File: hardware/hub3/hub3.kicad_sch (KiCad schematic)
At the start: 7 parts, among them J1 LCD0, J2 LCD1, J3 LCD2, U1 74HC138, U2 XIAO ESP32S3

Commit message: hub3: use the Ckmtw C132515 FFC connector, 44 mm board
C132515 has JLCPCB's own EasyEDA footprint, so the pads come from it
rather than from pixels of a drawing. Its body is 2.5 mm longer, so the
board grows to 44 mm to keep the corners clear. Move the 10 uF next to
the XIAO 5V pin.

route.py now starts each attempt from an unrouted copy that make.py
leaves in build/ with the project beside it (without it pcbnew used the
default net classes and saved them over the project), and when an
attempt is not clean it makes the board again: Freerouting routes the
same DSN the same way whatever its options, but each make.py run gives
a different DSN. Allow 7.5 mm of necked power track, about 2.5 mm per
connector.

Claude-Session: https://claude.ai/code/session_01QQqL2MiTqB6ZDq8JiNUdWg
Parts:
- J1, J2, J3: footprint cubic-earth:FFC_1.0mm_20P_Bottom_C2998680 -> cubic-earth:FFC_1.0mm_20P_Bottom_C132515; LCSC C2998680 -> C132515
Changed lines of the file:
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@@
 (property "Reference" "J1" (at 40.64 111.76 0) (effects (font (size 1.27 1.27))))
 (property "Value" "LCD0" (at 40.64 167.64 0) (effects (font (size 1.27 1.27))))
-(property "Footprint" "cubic-earth:FFC_1.0mm_20P_Bottom_C2998680" (at 40.64 139.70 0) (effects (font (size 1.27 1.27)) hide))
+(property "Footprint" "cubic-earth:FFC_1.0mm_20P_Bottom_C132515" (at 40.64 139.70 0) (effects (font (size 1.27 1.27)) hide))
 (property "Datasheet" "" (at 40.64 139.70 0) (effects (font (size 1.27 1.27)) hide))
-(property "LCSC" "C2998680" (at 40.64 139.70 0) (effects (font (size 1.27 1.27)) hide))
+(property "LCSC" "C132515" (at 40.64 139.70 0) (effects (font (size 1.27 1.27)) hide))
 (pin "1")
 (pin "2")
@@
 (pin "19")
 (pin "20")
-(instances (project "hub3" (path "/b9e327cf-b8af-4256-b178-5e44f1f45300" (reference "J1") (unit 1)))))
+(instances (project "hub3" (path "/f0ae39f4-92a4-45e5-bc8c-1e4964e93c33" (reference "J1") (unit 1)))))
 (global_label "GND" (shape passive) (at 35.56 115.57 180) (effects (font (size 1.27 1.27)) (justify right)))
 (global_label "GND" (shape passive) (at 35.56 118.11 180) (effects (font (size 1.27 1.27)) (justify right)))
@@
 (property "Reference" "J2" (at 99.06 111.76 0) (effects (font (size 1.27 1.27))))
 (property "Value" "LCD1" (at 99.06 167.64 0) (effects (font (size 1.27 1.27))))
-(property "Footprint" "cubic-earth:FFC_1.0mm_20P_Bottom_C2998680" (at 99.06 139.70 0) (effects (font (size 1.27 1.27)) hide))
+(property "Footprint" "cubic-earth:FFC_1.0mm_20P_Bottom_C132515" (at 99.06 139.70 0) (effects (font (size 1.27 1.27)) hide))
 (property "Datasheet" "" (at 99.06 139.70 0) (effects (font (size 1.27 1.27)) hide))
-(property "LCSC" "C2998680" (at 99.06 139.70 0) (effects (font (size 1.27 1.27)) hide))
+(property "LCSC" "C132515" (at 99.06 139.70 0) (effects (font (size 1.27 1.27)) hide))
 (pin "1")
 (pin "2")
@@
 (pin "19")
 (pin "20")
-(instances (project "hub3" (path "/b9e327cf-b8af-4256-b178-5e44f1f45300" (reference "J2") (unit 1)))))
+(instances (project "hub3" (path "/f0ae39f4-92a4-45e5-bc8c-1e4964e93c33" (reference "J2") (unit 1)))))
 (global_label "GND" (shape passive) (at 93.98 115.57 180) (effects (font (size 1.27 1.27)) (justify right)))
 (global_label "GND" (shape passive) (at 93.98 118.11 180) (effects (font (size 1.27 1.27)) (justify right)))
@@
 (property "Reference" "J3" (at 160.02 111.76 0) (effects (font (size 1.27 1.27))))
 (property "Value" "LCD2" (at 160.02 167.64 0) (effects (font (size 1.27 1.27))))
-(property "Footprint" "cubic-earth:FFC_1.0mm_20P_Bottom_C2998680" (at 160.02 139.70 0) (effects (font (size 1.27 1.27)) hide))
+(property "Footprint" "cubic-earth:FFC_1.0mm_20P_Bottom_C132515" (at 160.02 139.70 0) (effects (font (size 1.27 1.27)) hide))
 (property "Datasheet" "" (at 160.02 139.70 0) (effects (font (size 1.27 1.27)) hide))
-(property "LCSC" "C2998680" (at 160.02 139.70 0) (effects (font (size 1.27 1.27)) hide))
+(property "LCSC" "C132515" (at 160.02 139.70 0) (effects (font (size 1.27 1.27)) hide))
 (pin "1")
 (pin "2")
@@
 (pin "19")
 (pin "20")
-(instances (project "hub3" (path "/b9e327cf-b8af-4256-b178-5e44f1f45300" (reference "J3") (unit 1)))))
+(instances (project "hub3" (path "/f0ae39f4-92a4-45e5-bc8c-1e4964e93c33" (reference "J3") (unit 1)))))
 (global_label "GND" (shape passive) (at 154.94 115.57 180) (effects (font (size 1.27 1.27)) (justify right)))
 (global_label "GND" (shape passive) (at 154.94 118.11 180) (effects (font (size 1.27 1.27)) (justify right)))
@@
 (pin "8")
 (pin "9")
-(instances (project "hub3" (path "/b9e327cf-b8af-4256-b178-5e44f1f45300" (reference "U1") (unit 1)))))
+(instances (project "hub3" (path "/f0ae39f4-92a4-45e5-bc8c-1e4964e93c33" (reference "U1") (unit 1)))))
 (global_label "SEL_A" (shape passive) (at 119.38 60.96 180) (effects (font (size 1.27 1.27)) (justify right)))
 (global_label "LCD_CS2" (shape passive) (at 139.70 73.66 0) (effects (font (size 1.27 1.27)) (justify left)))
@@
 (pin "9")
 (pin "8")
-(instances (project "hub3" (path "/b9e327cf-b8af-4256-b178-5e44f1f45300" (reference "U2") (unit 1)))))
+(instances (project "hub3" (path "/f0ae39f4-92a4-45e5-bc8c-1e4964e93c33" (reference "U2") (unit 1)))))
 (global_label "SEL_A" (shape passive) (at 50.80 63.50 180) (effects (font (size 1.27 1.27)) (justify right)))
 (global_label "LCM_RESET" (shape passive) (at 50.80 66.04 180) (effects (font (size 1.27 1.27)) (justify right)))
@@
 (pin "1")
 (pin "2")
-(instances (project "hub3" (path "/b9e327cf-b8af-4256-b178-5e44f1f45300" (reference "C1") (unit 1)))))
+(instances (project "hub3" (path "/f0ae39f4-92a4-45e5-bc8c-1e4964e93c33" (reference "C1") (unit 1)))))
 (global_label "+3V3" (shape passive) (at 160.02 57.15 180) (effects (font (size 1.27 1.27)) (justify right)))
 (global_label "GND" (shape passive) (at 160.02 64.77 0) (effects (font (size 1.27 1.27)) (justify left)))
@@
 (pin "1")
 (pin "2")
-(instances (project "hub3" (path "/b9e327cf-b8af-4256-b178-5e44f1f45300" (reference "C2") (unit 1)))))
+(instances (project "hub3" (path "/f0ae39f4-92a4-45e5-bc8c-1e4964e93c33" (reference "C2") (unit 1)))))
 (global_label "+5V" (shape passive) (at 160.02 80.01 180) (effects (font (size 1.27 1.27)) (justify right)))
 (global_label "GND" (shape passive) (at 160.02 87.63 0) (effects (font (size 1.27 1.27)) (justify left)))

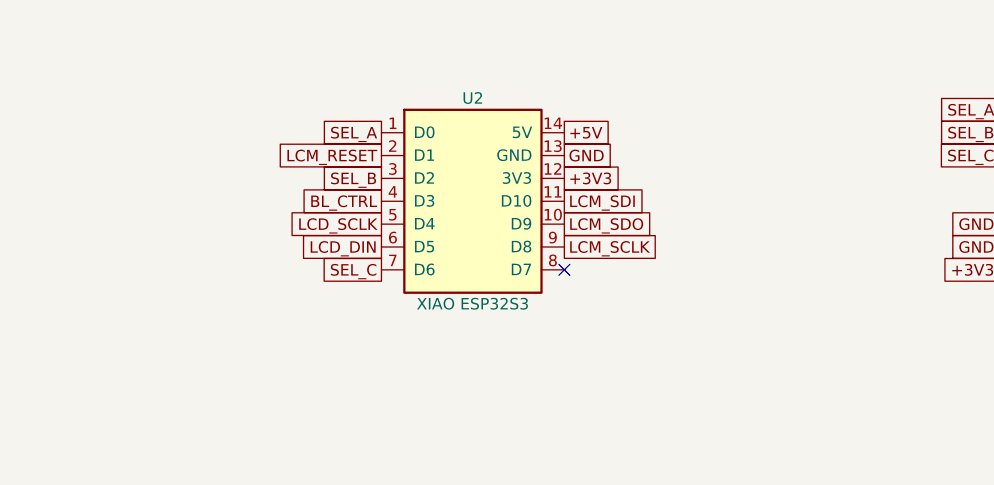
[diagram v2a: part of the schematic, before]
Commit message: hub3: assemble the XIAO's two pin sockets too
Replace the XIAO footprint with two 1x7 2.54 mm female sockets (J4, J5,
XFCN PM254V-11-07-H85, LCSC C2832270) for JLCPCB to fit. The XIAO
stays on the schematic but off the board; a board-only outline marks
where it sits and which row is D0 and which 5V. The placement file
gives the sockets' pad centre, since their origin is on pin 1. A test
checks the rows are 15.24 mm apart with D0 and 5V at the USB end.

Claude-Session: https://claude.ai/code/session_01QQqL2MiTqB6ZDq8JiNUdWg
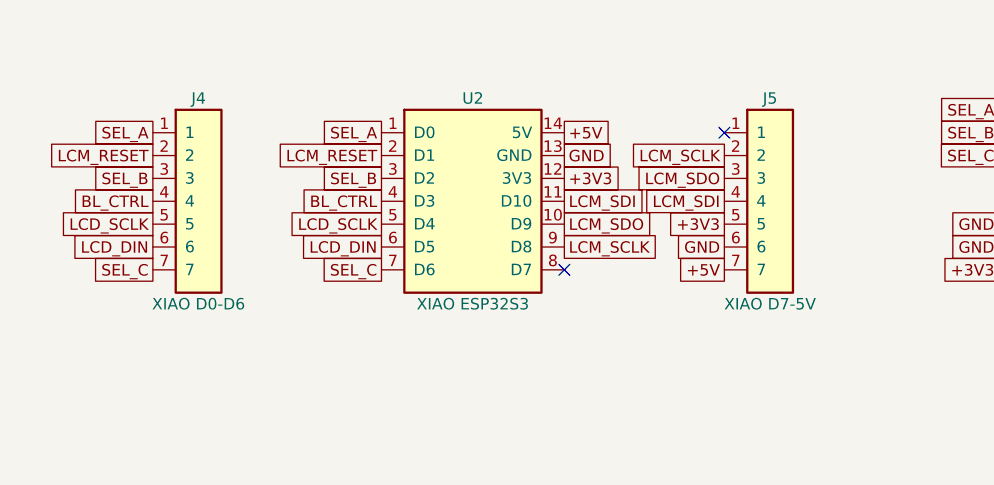
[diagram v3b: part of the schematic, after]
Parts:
- added J4: XIAO D0-D6, Connector_PinSocket_2.54mm:PinSocket_1x07_P2.54mm_Vertical, symbol cubic-earth:Socket_1x07
- added J5: XIAO D7-5V, Connector_PinSocket_2.54mm:PinSocket_1x07_P2.54mm_Vertical, symbol cubic-earth:Socket_1x07
- U2: footprint cubic-earth:XIAO_Socket_2x7_P2.54mm -> (none); now left out of the parts list
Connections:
- net +3V3: now also J5.5
- net +5V: now also J5.7
- net BL_CTRL: now also J4.4
- net GND: now also J5.6
- net LCD_DIN: now also J4.6
- net LCD_SCLK: now also J4.5
- net LCM_RESET: now also J4.2
- net LCM_SCLK: now also J5.2
- net LCM_SDI: now also J5.4
- net LCM_SDO: now also J5.3
- net SEL_A: now also J4.1
- net SEL_B: now also J4.3
- net SEL_C: now also J4.7
- no-connect marks 24 -> 25
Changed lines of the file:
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@@
 (pin "19")
 (pin "20")
-(instances (project "hub3" (path "/f0ae39f4-92a4-45e5-bc8c-1e4964e93c33" (reference "J1") (unit 1)))))
+(instances (project "hub3" (path "/a8cdc18e-1b7c-4f21-9802-1abcb25c4a52" (reference "J1") (unit 1)))))
 (global_label "GND" (shape passive) (at 35.56 115.57 180) (effects (font (size 1.27 1.27)) (justify right)))
 (global_label "GND" (shape passive) (at 35.56 118.11 180) (effects (font (size 1.27 1.27)) (justify right)))
@@
 (pin "19")
 (pin "20")
-(instances (project "hub3" (path "/f0ae39f4-92a4-45e5-bc8c-1e4964e93c33" (reference "J2") (unit 1)))))
+(instances (project "hub3" (path "/a8cdc18e-1b7c-4f21-9802-1abcb25c4a52" (reference "J2") (unit 1)))))
 (global_label "GND" (shape passive) (at 93.98 115.57 180) (effects (font (size 1.27 1.27)) (justify right)))
 (global_label "GND" (shape passive) (at 93.98 118.11 180) (effects (font (size 1.27 1.27)) (justify right)))
@@
 (pin "19")
 (pin "20")
-(instances (project "hub3" (path "/f0ae39f4-92a4-45e5-bc8c-1e4964e93c33" (reference "J3") (unit 1)))))
+(instances (project "hub3" (path "/a8cdc18e-1b7c-4f21-9802-1abcb25c4a52" (reference "J3") (unit 1)))))
 (global_label "GND" (shape passive) (at 154.94 115.57 180) (effects (font (size 1.27 1.27)) (justify right)))
 (global_label "GND" (shape passive) (at 154.94 118.11 180) (effects (font (size 1.27 1.27)) (justify right)))
@@
 (pin "8")
 (pin "9")
-(instances (project "hub3" (path "/f0ae39f4-92a4-45e5-bc8c-1e4964e93c33" (reference "U1") (unit 1)))))
+(instances (project "hub3" (path "/a8cdc18e-1b7c-4f21-9802-1abcb25c4a52" (reference "U1") (unit 1)))))
 (global_label "SEL_A" (shape passive) (at 119.38 60.96 180) (effects (font (size 1.27 1.27)) (justify right)))
 (global_label "LCD_CS2" (shape passive) (at 139.70 73.66 0) (effects (font (size 1.27 1.27)) (justify left)))
@@
 (global_label "GND" (shape passive) (at 129.54 83.82 0) (effects (font (size 1.27 1.27)) (justify left)))
 (no_connect (at 139.70 76.20))
-(symbol (lib_id "cubic-earth:XIAO_ESP32S3") (at 60.96 71.12 0) (unit 1) (exclude_from_sim no) (in_bom yes) (on_board yes) (dnp no)
+(symbol (lib_id "cubic-earth:XIAO_ESP32S3") (at 60.96 71.12 0) (unit 1) (exclude_from_sim no) (in_bom no) (on_board no) (dnp no)
 (property "Reference" "U2" (at 60.96 59.69 0) (effects (font (size 1.27 1.27))))
 (property "Value" "XIAO ESP32S3" (at 60.96 82.55 0) (effects (font (size 1.27 1.27))))
-(property "Footprint" "cubic-earth:XIAO_Socket_2x7_P2.54mm" (at 60.96 71.12 0) (effects (font (size 1.27 1.27)) hide))
+(property "Footprint" "" (at 60.96 71.12 0) (effects (font (size 1.27 1.27)) hide))
 (property "Datasheet" "" (at 60.96 71.12 0) (effects (font (size 1.27 1.27)) hide))
 (pin "1")
@@
 (pin "9")
 (pin "8")
-(instances (project "hub3" (path "/f0ae39f4-92a4-45e5-bc8c-1e4964e93c33" (reference "U2") (unit 1)))))
+(instances (project "hub3" (path "/a8cdc18e-1b7c-4f21-9802-1abcb25c4a52" (reference "U2") (unit 1)))))
 (global_label "SEL_A" (shape passive) (at 50.80 63.50 180) (effects (font (size 1.27 1.27)) (justify right)))
 (global_label "LCM_RESET" (shape passive) (at 50.80 66.04 180) (effects (font (size 1.27 1.27)) (justify right)))
@@
 (global_label "LCM_SCLK" (shape passive) (at 71.12 76.20 0) (effects (font (size 1.27 1.27)) (justify left)))
 (no_connect (at 71.12 78.74))
+(symbol (lib_id "cubic-earth:Socket_1x07") (at 30.48 71.12 0) (unit 1) (exclude_from_sim no) (in_bom yes) (on_board yes) (dnp no)
+(property "Reference" "J4" (at 30.48 59.69 0) (effects (font (size 1.27 1.27))))
+(property "Value" "XIAO D0-D6" (at 30.48 82.55 0) (effects (font (size 1.27 1.27))))
+(property "Footprint" "Connector_PinSocket_2.54mm:PinSocket_1x07_P2.54mm_Vertical" (at 30.48 71.12 0) (effects (font (size 1.27 1.27)) hide))
+(property "Datasheet" "" (at 30.48 71.12 0) (effects (font (size 1.27 1.27)) hide))
+(property "LCSC" "C2832270" (at 30.48 71.12 0) (effects (font (size 1.27 1.27)) hide))
+(pin "1")
+(pin "2")
+(pin "3")
+(pin "4")
+(pin "5")
+(pin "6")
+(pin "7")
+(instances (project "hub3" (path "/a8cdc18e-1b7c-4f21-9802-1abcb25c4a52" (reference "J4") (unit 1)))))
+(global_label "SEL_A" (shape passive) (at 25.40 63.50 180) (effects (font (size 1.27 1.27)) (justify right)))
+(global_label "LCM_RESET" (shape passive) (at 25.40 66.04 180) (effects (font (size 1.27 1.27)) (justify right)))
+(global_label "SEL_B" (shape passive) (at 25.40 68.58 180) (effects (font (size 1.27 1.27)) (justify right)))
+(global_label "BL_CTRL" (shape passive) (at 25.40 71.12 180) (effects (font (size 1.27 1.27)) (justify right)))
+(global_label "LCD_SCLK" (shape passive) (at 25.40 73.66 180) (effects (font (size 1.27 1.27)) (justify right)))
+(global_label "LCD_DIN" (shape passive) (at 25.40 76.20 180) (effects (font (size 1.27 1.27)) (justify right)))
+(global_label "SEL_C" (shape passive) (at 25.40 78.74 180) (effects (font (size 1.27 1.27)) (justify right)))
+(symbol (lib_id "cubic-earth:Socket_1x07") (at 93.98 71.12 0) (unit 1) (exclude_from_sim no) (in_bom yes) (on_board yes) (dnp no)
+(property "Reference" "J5" (at 93.98 59.69 0) (effects (font (size 1.27 1.27))))
+(property "Value" "XIAO D7-5V" (at 93.98 82.55 0) (effects (font (size 1.27 1.27))))
+(property "Footprint" "Connector_PinSocket_2.54mm:PinSocket_1x07_P2.54mm_Vertical" (at 93.98 71.12 0) (effects (font (size 1.27 1.27)) hide))
+(property "Datasheet" "" (at 93.98 71.12 0) (effects (font (size 1.27 1.27)) hide))
+(property "LCSC" "C2832270" (at 93.98 71.12 0) (effects (font (size 1.27 1.27)) hide))
+(pin "1")
+(pin "2")
+(pin "3")
+(pin "4")
+(pin "5")
+(pin "6")
+(pin "7")
+(instances (project "hub3" (path "/a8cdc18e-1b7c-4f21-9802-1abcb25c4a52" (reference "J5") (unit 1)))))
+(no_connect (at 88.90 63.50))
+(global_label "LCM_SCLK" (shape passive) (at 88.90 66.04 180) (effects (font (size 1.27 1.27)) (justify right)))
+(global_label "LCM_SDO" (shape passive) (at 88.90 68.58 180) (effects (font (size 1.27 1.27)) (justify right)))
+(global_label "LCM_SDI" (shape passive) (at 88.90 71.12 180) (effects (font (size 1.27 1.27)) (justify right)))
+(global_label "+3V3" (shape passive) (at 88.90 73.66 180) (effects (font (size 1.27 1.27)) (justify right)))
+(global_label "GND" (shape passive) (at 88.90 76.20 180) (effects (font (size 1.27 1.27)) (justify right)))
+(global_label "+5V" (shape passive) (at 88.90 78.74 180) (effects (font (size 1.27 1.27)) (justify right)))
 (symbol (lib_id "Device:C") (at 160.02 60.96 0) (unit 1) (exclude_from_sim no) (in_bom yes) (on_board yes) (dnp no)
 (property "Reference" "C1" (at 160.02 53.34 0) (effects (font (size 1.27 1.27))))
@@
 (pin "1")
 (pin "2")
-(instances (project "hub3" (path "/f0ae39f4-92a4-45e5-bc8c-1e4964e93c33" (reference "C1") (unit 1)))))
+(instances (project "hub3" (path "/a8cdc18e-1b7c-4f21-9802-1abcb25c4a52" (reference "C1") (unit 1)))))
 (global_label "+3V3" (shape passive) (at 160.02 57.15 180) (effects (font (size 1.27 1.27)) (justify right)))
 (global_label "GND" (shape passive) (at 160.02 64.77 0) (effects (font (size 1.27 1.27)) (justify left)))
@@
 (pin "1")
 (pin "2")
-(instances (project "hub3" (path "/f0ae39f4-92a4-45e5-bc8c-1e4964e93c33" (reference "C2") (unit 1)))))
+(instances (project "hub3" (path "/a8cdc18e-1b7c-4f21-9802-1abcb25c4a52" (reference "C2") (unit 1)))))
 (global_label "+5V" (shape passive) (at 160.02 80.01 180) (effects (font (size 1.27 1.27)) (justify right)))
 (global_label "GND" (shape passive) (at 160.02 87.63 0) (effects (font (size 1.27 1.27)) (justify left)))
